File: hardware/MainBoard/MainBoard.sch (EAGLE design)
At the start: 220 parts, among them J1 CON-71741-2184-BOT, J2 CON-71741-2184-TOP, J3 CON-FTSH-105-01-L-DV-K, J4 CON-ZX62R-B-5P, J5 CON-SMA, J6 CON-SMA, J7 CON-RJ45-J0G-0007NL, J8 SWITCH-CJS-1200-1200, M1 MOUNT-HOLE3.3, M2 MOUNT-HOLE3.3, M3 MOUNT-HOLE3.3, M4 MOUNT-HOLE3.3, M5 FIDUCIAL1X2, M6 FIDUCIAL1X2, M7 FIDUCIAL1X2, M8 FIDUCIAL1X2, Q1 MMBT3904, SW1 SWITCH-KSC-201J, SW2 SWITCH-KSC-201J, U1 A2F500M3G-FG256, U2 MAX19706-T4877-4, U3 MAX19706-T4877-4, U4 USBLC6-2SC6, U5 FT232HL, U6 DP83848C-VBH48A, U7 93LC56BT-OT, U8 DS1818-10-SOT-23, U9 LMV112, X1 FOX924B, X2 ECX-31B, X3 ASEM1-C, X5 ECX-42-120

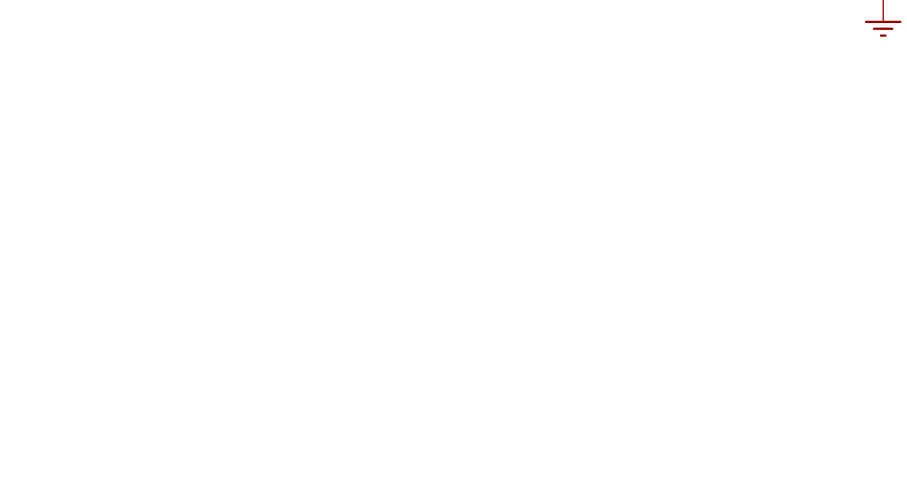
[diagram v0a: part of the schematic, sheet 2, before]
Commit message: Added decoupling capacitor to 1.5V supplies (3.3V IOB supply capacitors still missing).
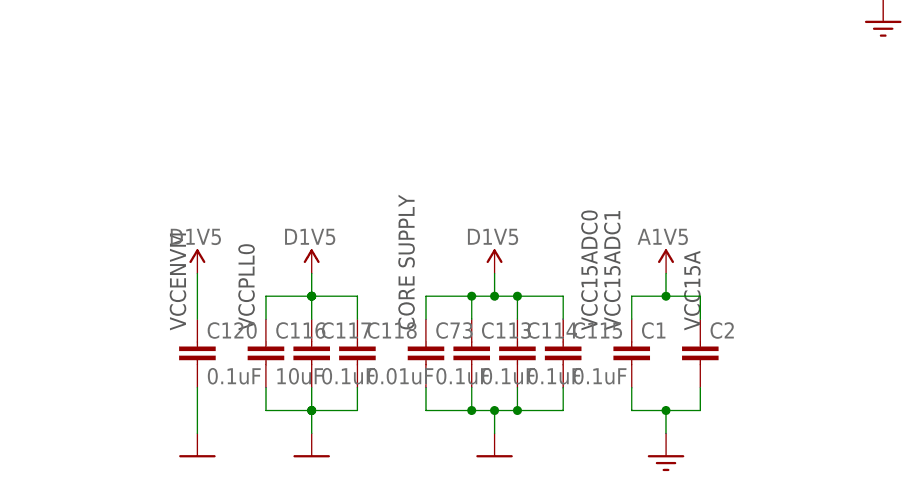
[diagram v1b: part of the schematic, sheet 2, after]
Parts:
- added C1, C2: (no value), MainBoard:C0402
- added C113, C114, C115, C117, C120, C73: 0.1uF, MainBoard:C0402
- added C116: 10uF, MainBoard:C0402
- added C118: 0.01uF, MainBoard:C0402
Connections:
- net A1V5: now also C1.1, C2.1
- net AGND: now also C1.2, C2.2
- net D1V5: now also C113.1, C114.1, C115.1, C116.1, C117.1, C118.1, C120.1, C73.1
- net DGND: now also C113.2, C114.2, C115.2, C116.2, C117.2, C118.2, C120.2, C73.2
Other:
- note added: "CORE SUPPLY"
- note added: "VCC15A"
- note added: "VCC15ADC0"
- note added: "VCC15ADC1"
- note added: "VCCENVM"
- note added: "VCCPLL0"
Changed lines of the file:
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@@
 <part name="U$69" library="MainBoard" deviceset="D3V3" device=""/>
 <part name="U$80" library="MainBoard" deviceset="D1V5" device=""/>
+<part name="C1" library="MainBoard" deviceset="C" device="0402"/>
+<part name="C2" library="MainBoard" deviceset="C" device="0402"/>
+<part name="U$81" library="MainBoard" deviceset="AGND" device=""/>
+<part name="U$88" library="MainBoard" deviceset="A1V5" device=""/>
+<part name="U$92" library="MainBoard" deviceset="D1V5" device=""/>
+<part name="C73" library="MainBoard" deviceset="C" device="0402" value="0.1uF"/>
+<part name="C113" library="MainBoard" deviceset="C" device="0402" value="0.1uF"/>
+<part name="C114" library="MainBoard" deviceset="C" device="0402" value="0.1uF"/>
+<part name="C115" library="MainBoard" deviceset="C" device="0402" value="0.1uF"/>
+<part name="U$126" library="MainBoard" deviceset="DGND" device=""/>
+<part name="U$135" library="MainBoard" deviceset="D1V5" device=""/>
+<part name="C116" library="MainBoard" deviceset="C" device="0402" value="10uF"/>
+<part name="C117" library="MainBoard" deviceset="C" device="0402" value="0.1uF"/>
+<part name="C118" library="MainBoard" deviceset="C" device="0402" value="0.01uF"/>
+<part name="U$136" library="MainBoard" deviceset="DGND" device=""/>
+<part name="U$137" library="MainBoard" deviceset="D1V5" device=""/>
+<part name="C120" library="MainBoard" deviceset="C" device="0402" value="0.1uF"/>
+<part name="U$138" library="MainBoard" deviceset="DGND" device=""/>
 </parts>
 <sheets>
@@
 <text x="182.88" y="111.76" size="2.54" layer="97">ANALOG-SUPPLY</text>
 <text x="53.34" y="78.74" size="50.8" layer="208">SUP</text>
-<rectangle x1="218.44" y1="143.51" x2="226.06" y2="146.05" layer="101"/>
+<rectangle x1="223.52" y1="143.51" x2="231.14" y2="146.05" layer="101"/>
 <rectangle x1="167.64" y1="120.65" x2="175.26" y2="123.19" layer="101"/>
+<text x="138.43" y="31.75" size="1.778" layer="97" rot="R90">VCC15ADC0</text>
+<text x="140.97" y="31.75" size="1.778" layer="97" rot="R90">VCC15ADC1</text>
+<text x="149.86" y="31.75" size="1.778" layer="97" rot="R90">VCC15A</text>
+<rectangle x1="137.16" y1="12.7" x2="157.48" y2="48.26" layer="116"/>
+<text x="118.11" y="31.75" size="1.778" layer="97" rot="R90">CORE SUPPLY</text>
+<text x="100.33" y="31.75" size="1.778" layer="97" rot="R90">VCCPLL0</text>
+<text x="92.71" y="31.75" size="1.778" layer="97" rot="R90">VCCENVM</text>
+<rectangle x1="86.36" y1="15.24" x2="116.84" y2="45.72" layer="116"/>
 </plain>
 <instances>
@@
 <instance part="U$69" gate="G$1" x="162.56" y="124.46"/>
 <instance part="U$80" gate="G$1" x="233.68" y="147.32"/>
+<instance part="C1" gate="G$1" x="142.24" y="30.48"/>
+<instance part="C2" gate="G$1" x="149.86" y="30.48"/>
+<instance part="U$81" gate="G$1" x="146.05" y="17.78"/>
+<instance part="U$88" gate="G$1" x="146.05" y="38.1"/>
+<instance part="U$92" gate="G$1" x="127" y="38.1"/>
+<instance part="C73" gate="G$1" x="119.38" y="30.48"/>
+<instance part="C113" gate="G$1" x="124.46" y="30.48"/>
+<instance part="C114" gate="G$1" x="129.54" y="30.48"/>
+<instance part="C115" gate="G$1" x="134.62" y="30.48"/>
+<instance part="U$126" gate="G$1" x="127" y="17.78"/>
+<instance part="U$135" gate="G$1" x="106.68" y="38.1"/>
+<instance part="C116" gate="G$1" x="101.6" y="30.48"/>
+<instance part="C117" gate="G$1" x="106.68" y="30.48"/>
+<instance part="C118" gate="G$1" x="111.76" y="30.48"/>
+<instance part="U$136" gate="G$1" x="106.68" y="17.78"/>
+<instance part="U$137" gate="G$1" x="93.98" y="38.1"/>
+<instance part="C120" gate="G$1" x="93.98" y="30.48"/>
+<instance part="U$138" gate="G$1" x="93.98" y="17.78"/>
 </instances>
 <busses>
@@
 <junction x="149.86" y="101.6"/>
 </segment>
+<segment>
+<pinref part="C73" gate="G$1" pin="2"/>
+<wire x1="119.38" y1="25.4" x2="119.38" y2="22.86" width="0.1524" layer="91"/>
+<wire x1="119.38" y1="22.86" x2="124.46" y2="22.86" width="0.1524" layer="91"/>
+<pinref part="C115" gate="G$1" pin="2"/>
+<wire x1="124.46" y1="22.86" x2="127" y2="22.86" width="0.1524" layer="91"/>
+<wire x1="127" y1="22.86" x2="129.54" y2="22.86" width="0.1524" layer="91"/>
+<wire x1="129.54" y1="22.86" x2="134.62" y2="22.86" width="0.1524" layer="91"/>
+<wire x1="134.62" y1="22.86" x2="134.62" y2="25.4" width="0.1524" layer="91"/>
+<pinref part="C113" gate="G$1" pin="2"/>
+<wire x1="124.46" y1="25.4" x2="124.46" y2="22.86" width="0.1524" layer="91"/>
+<pinref part="C114" gate="G$1" pin="2"/>
+<wire x1="129.54" y1="25.4" x2="129.54" y2="22.86" width="0.1524" layer="91"/>
+<wire x1="127" y1="22.86" x2="127" y2="20.32" width="0.1524" layer="91"/>
+<pinref part="U$126" gate="G$1" pin="DGND"/>
+<junction x="124.46" y="22.86"/>
+<junction x="127" y="22.86"/>
+<junction x="129.54" y="22.86"/>
+</segment>
+<segment>
+<pinref part="C116" gate="G$1" pin="2"/>
+<wire x1="101.6" y1="25.4" x2="101.6" y2="22.86" width="0.1524" layer="91"/>
+<wire x1="101.6" y1="22.86" x2="106.68" y2="22.86" width="0.1524" layer="91"/>
+<wire x1="106.68" y1="22.86" x2="111.76" y2="22.86" width="0.1524" layer="91"/>
+<pinref part="C117" gate="G$1" pin="2"/>
+<wire x1="106.68" y1="25.4" x2="106.68" y2="22.86" width="0.1524" layer="91"/>
+<pinref part="C118" gate="G$1" pin="2"/>
+<wire x1="111.76" y1="25.4" x2="111.76" y2="22.86" width="0.1524" layer="91"/>
+<wire x1="106.68" y1="22.86" x2="106.68" y2="20.32" width="0.1524" layer="91"/>
+<pinref part="U$136" gate="G$1" pin="DGND"/>
+<junction x="106.68" y="22.86"/>
+<junction x="106.68" y="22.86"/>
+</segment>
+<segment>
+<pinref part="C120" gate="G$1" pin="2"/>
+<wire x1="93.98" y1="25.4" x2="93.98" y2="20.32" width="0.1524" layer="91"/>
+<pinref part="U$138" gate="G$1" pin="DGND"/>
+</segment>
 </net>
 <net name="D1V5" class="0">
@@
 <wire x1="233.68" y1="144.78" x2="233.68" y2="147.32" width="0.1524" layer="91"/>
 <pinref part="U$80" gate="G$1" pin="D1V5"/>
+</segment>
+<segment>
+<pinref part="U$92" gate="G$1" pin="D1V5"/>
+<wire x1="127" y1="38.1" x2="127" y2="35.56" width="0.1524" layer="91"/>
+<wire x1="127" y1="35.56" x2="124.46" y2="35.56" width="0.1524" layer="91"/>
+<wire x1="124.46" y1="35.56" x2="119.38" y2="35.56" width="0.1524" layer="91"/>
+<wire x1="127" y1="35.56" x2="129.54" y2="35.56" width="0.1524" layer="91"/>
+<pinref part="C73" gate="G$1" pin="1"/>
+<wire x1="129.54" y1="35.56" x2="134.62" y2="35.56" width="0.1524" layer="91"/>
+<wire x1="119.38" y1="33.02" x2="119.38" y2="35.56" width="0.1524" layer="91"/>
+<pinref part="C113" gate="G$1" pin="1"/>
+<wire x1="124.46" y1="33.02" x2="124.46" y2="35.56" width="0.1524" layer="91"/>
+<pinref part="C114" gate="G$1" pin="1"/>
+<wire x1="129.54" y1="33.02" x2="129.54" y2="35.56" width="0.1524" layer="91"/>
+<pinref part="C115" gate="G$1" pin="1"/>
+<wire x1="134.62" y1="33.02" x2="134.62" y2="35.56" width="0.1524" layer="91"/>
+<junction x="124.46" y="35.56"/>
+<junction x="127" y="35.56"/>
+<junction x="129.54" y="35.56"/>
+</segment>
+<segment>
+<pinref part="U$135" gate="G$1" pin="D1V5"/>
+<wire x1="106.68" y1="38.1" x2="106.68" y2="35.56" width="0.1524" layer="91"/>
+<wire x1="106.68" y1="35.56" x2="101.6" y2="35.56" width="0.1524" layer="91"/>
+<wire x1="106.68" y1="35.56" x2="111.76" y2="35.56" width="0.1524" layer="91"/>
+<pinref part="C116" gate="G$1" pin="1"/>
+<wire x1="101.6" y1="33.02" x2="101.6" y2="35.56" width="0.1524" layer="91"/>
+<pinref part="C117" gate="G$1" pin="1"/>
+<wire x1="106.68" y1="33.02" x2="106.68" y2="35.56" width="0.1524" layer="91"/>
+<pinref part="C118" gate="G$1" pin="1"/>
+<wire x1="111.76" y1="33.02" x2="111.76" y2="35.56" width="0.1524" layer="91"/>
+<junction x="106.68" y="35.56"/>
+<junction x="106.68" y="35.56"/>
+</segment>
+<segment>
+<pinref part="U$137" gate="G$1" pin="D1V5"/>
+<pinref part="C120" gate="G$1" pin="1"/>
+<wire x1="93.98" y1="33.02" x2="93.98" y2="38.1" width="0.1524" layer="91"/>
 </segment>
 </net>
@@
 <junction x="226.06" y="71.12"/>
 </segment>
+<segment>
+<pinref part="C2" gate="G$1" pin="2"/>
+<pinref part="C1" gate="G$1" pin="2"/>
+<wire x1="142.24" y1="25.4" x2="142.24" y2="22.86" width="0.1524" layer="91"/>
+<wire x1="142.24" y1="22.86" x2="146.05" y2="22.86" width="0.1524" layer="91"/>
+<wire x1="146.05" y1="22.86" x2="149.86" y2="22.86" width="0.1524" layer="91"/>
+<wire x1="149.86" y1="22.86" x2="149.86" y2="25.4" width="0.1524" layer="91"/>
+<pinref part="U$81" gate="G$1" pin="AGND"/>
+<wire x1="146.05" y1="20.32" x2="146.05" y2="22.86" width="0.1524" layer="91"/>
+<junction x="146.05" y="22.86"/>
+</segment>
 </net>
 <net name="A1V5" class="0">
@@
 <junction x="226.06" y="157.48"/>
 </segment>
+<segment>
+<pinref part="C1" gate="G$1" pin="1"/>
+<wire x1="142.24" y1="33.02" x2="142.24" y2="35.56" width="0.1524" layer="91"/>
+<wire x1="142.24" y1="35.56" x2="146.05" y2="35.56" width="0.1524" layer="91"/>
+<wire x1="146.05" y1="35.56" x2="146.05" y2="38.1" width="0.1524" layer="91"/>
+<pinref part="U$88" gate="G$1" pin="A1V5"/>
+<pinref part="C2" gate="G$1" pin="1"/>
+<wire x1="149.86" y1="33.02" x2="149.86" y2="35.56" width="0.1524" layer="91"/>
+<wire x1="149.86" y1="35.56" x2="146.05" y2="35.56" width="0.1524" layer="91"/>
+<junction x="146.05" y="35.56"/>
+</segment>
 </net>

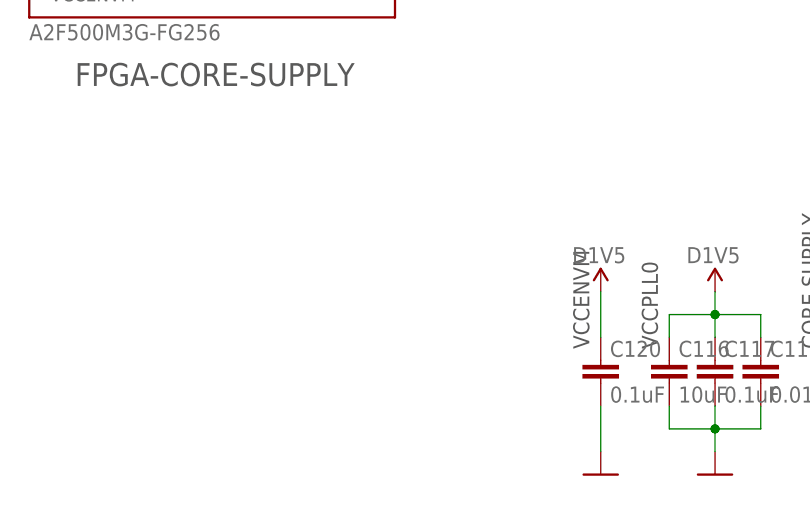
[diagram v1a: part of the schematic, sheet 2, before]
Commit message: 
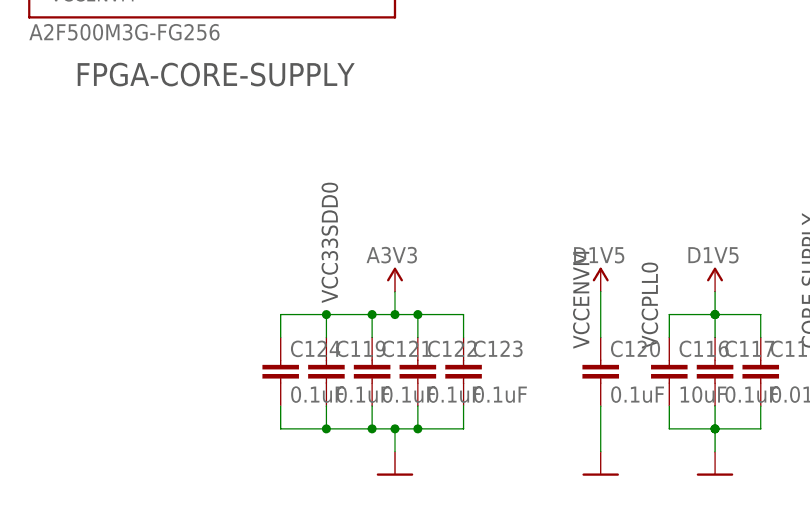
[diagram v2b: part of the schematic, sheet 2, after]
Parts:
- added C119, C121, C122, C123, C124: 0.1uF, MainBoard:C0402
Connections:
- net A3V3: now also C119.1, C121.1, C122.1, C123.1, C124.1
- net DGND: now also C119.2, C121.2, C122.2, C123.2, C124.2
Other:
- note added: "VCC33SDD0"
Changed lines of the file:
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@@
 <part name="C120" library="MainBoard" deviceset="C" device="0402" value="0.1uF"/>
 <part name="U$138" library="MainBoard" deviceset="DGND" device=""/>
+<part name="C119" library="MainBoard" deviceset="C" device="0402" value="0.1uF"/>
+<part name="C121" library="MainBoard" deviceset="C" device="0402" value="0.1uF"/>
+<part name="C122" library="MainBoard" deviceset="C" device="0402" value="0.1uF"/>
+<part name="C123" library="MainBoard" deviceset="C" device="0402" value="0.1uF"/>
+<part name="U$140" library="MainBoard" deviceset="DGND" device=""/>
+<part name="U$139" library="MainBoard" deviceset="A3V3" device=""/>
+<part name="C124" library="MainBoard" deviceset="C" device="0402" value="0.1uF"/>
 </parts>
 <sheets>
@@
 <text x="92.71" y="31.75" size="1.778" layer="97" rot="R90">VCCENVM</text>
 <rectangle x1="86.36" y1="15.24" x2="116.84" y2="45.72" layer="116"/>
+<rectangle x1="12.7" y1="66.04" x2="88.9" y2="99.06" layer="116"/>
+<rectangle x1="200.66" y1="147.32" x2="228.6" y2="165.1" layer="116"/>
+<rectangle x1="96.52" y1="83.82" x2="154.94" y2="165.1" layer="116"/>
+<rectangle x1="165.1" y1="53.34" x2="236.22" y2="104.14" layer="116"/>
+<rectangle x1="218.44" y1="109.22" x2="236.22" y2="124.46" layer="116"/>
+<text x="64.77" y="36.83" size="1.778" layer="97" rot="R90">VCC33SDD0</text>
 </plain>
 <instances>
@@
 <instance part="C120" gate="G$1" x="93.98" y="30.48"/>
 <instance part="U$138" gate="G$1" x="93.98" y="17.78"/>
+<instance part="C119" gate="G$1" x="63.5" y="30.48"/>
+<instance part="C121" gate="G$1" x="68.58" y="30.48"/>
+<instance part="C122" gate="G$1" x="73.66" y="30.48"/>
+<instance part="C123" gate="G$1" x="78.74" y="30.48"/>
+<instance part="U$140" gate="G$1" x="71.12" y="17.78"/>
+<instance part="U$139" gate="G$1" x="71.12" y="38.1"/>
+<instance part="C124" gate="G$1" x="58.42" y="30.48"/>
 </instances>
 <busses>
@@
 <pinref part="U$138" gate="G$1" pin="DGND"/>
 </segment>
+<segment>
+<pinref part="C119" gate="G$1" pin="2"/>
+<wire x1="63.5" y1="25.4" x2="63.5" y2="22.86" width="0.1524" layer="91"/>
+<wire x1="63.5" y1="22.86" x2="68.58" y2="22.86" width="0.1524" layer="91"/>
+<pinref part="C123" gate="G$1" pin="2"/>
+<wire x1="68.58" y1="22.86" x2="71.12" y2="22.86" width="0.1524" layer="91"/>
+<wire x1="71.12" y1="22.86" x2="73.66" y2="22.86" width="0.1524" layer="91"/>
+<wire x1="73.66" y1="22.86" x2="78.74" y2="22.86" width="0.1524" layer="91"/>
+<wire x1="78.74" y1="22.86" x2="78.74" y2="25.4" width="0.1524" layer="91"/>
+<pinref part="C121" gate="G$1" pin="2"/>
+<wire x1="68.58" y1="25.4" x2="68.58" y2="22.86" width="0.1524" layer="91"/>
+<pinref part="C122" gate="G$1" pin="2"/>
+<wire x1="73.66" y1="25.4" x2="73.66" y2="22.86" width="0.1524" layer="91"/>
+<wire x1="71.12" y1="22.86" x2="71.12" y2="20.32" width="0.1524" layer="91"/>
+<pinref part="U$140" gate="G$1" pin="DGND"/>
+<junction x="68.58" y="22.86"/>
+<junction x="71.12" y="22.86"/>
+<junction x="73.66" y="22.86"/>
+<pinref part="C124" gate="G$1" pin="2"/>
+<wire x1="58.42" y1="25.4" x2="58.42" y2="22.86" width="0.1524" layer="91"/>
+<wire x1="58.42" y1="22.86" x2="63.5" y2="22.86" width="0.1524" layer="91"/>
+<junction x="63.5" y="22.86"/>
+</segment>
 </net>
 <net name="D1V5" class="0">
@@
 <junction x="170.18" y="137.16"/>
 </segment>
+<segment>
+<wire x1="71.12" y1="38.1" x2="71.12" y2="35.56" width="0.1524" layer="91"/>
+<wire x1="71.12" y1="35.56" x2="68.58" y2="35.56" width="0.1524" layer="91"/>
+<wire x1="68.58" y1="35.56" x2="63.5" y2="35.56" width="0.1524" layer="91"/>
+<wire x1="71.12" y1="35.56" x2="73.66" y2="35.56" width="0.1524" layer="91"/>
+<pinref part="C119" gate="G$1" pin="1"/>
+<wire x1="73.66" y1="35.56" x2="78.74" y2="35.56" width="0.1524" layer="91"/>
+<wire x1="63.5" y1="33.02" x2="63.5" y2="35.56" width="0.1524" layer="91"/>
+<pinref part="C121" gate="G$1" pin="1"/>
+<wire x1="68.58" y1="33.02" x2="68.58" y2="35.56" width="0.1524" layer="91"/>
+<pinref part="C122" gate="G$1" pin="1"/>
+<wire x1="73.66" y1="33.02" x2="73.66" y2="35.56" width="0.1524" layer="91"/>
+<pinref part="C123" gate="G$1" pin="1"/>
+<wire x1="78.74" y1="33.02" x2="78.74" y2="35.56" width="0.1524" layer="91"/>
+<junction x="68.58" y="35.56"/>
+<junction x="71.12" y="35.56"/>
+<junction x="73.66" y="35.56"/>
+<pinref part="U$139" gate="G$1" pin="A3V3"/>
+<pinref part="C124" gate="G$1" pin="1"/>
+<wire x1="58.42" y1="33.02" x2="58.42" y2="35.56" width="0.1524" layer="91"/>
+<wire x1="58.42" y1="35.56" x2="63.5" y2="35.56" width="0.1524" layer="91"/>
+<junction x="63.5" y="35.56"/>
+</segment>
 </net>

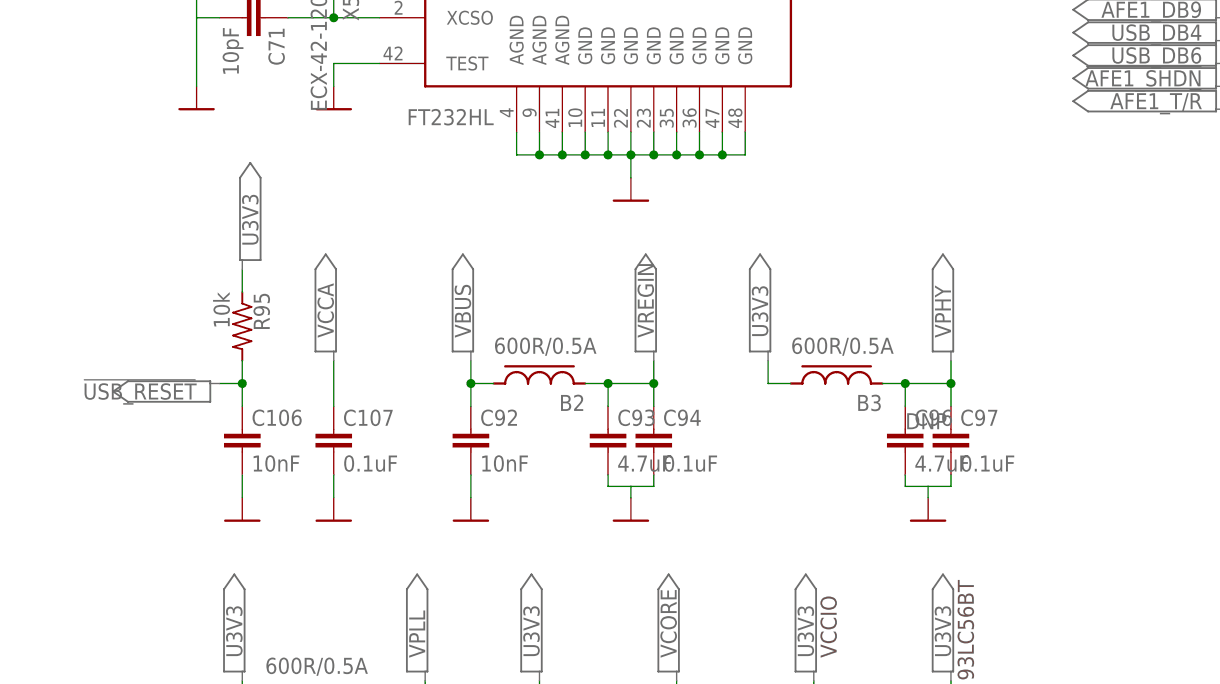
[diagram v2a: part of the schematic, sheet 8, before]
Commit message: USB routing optimization back-up.
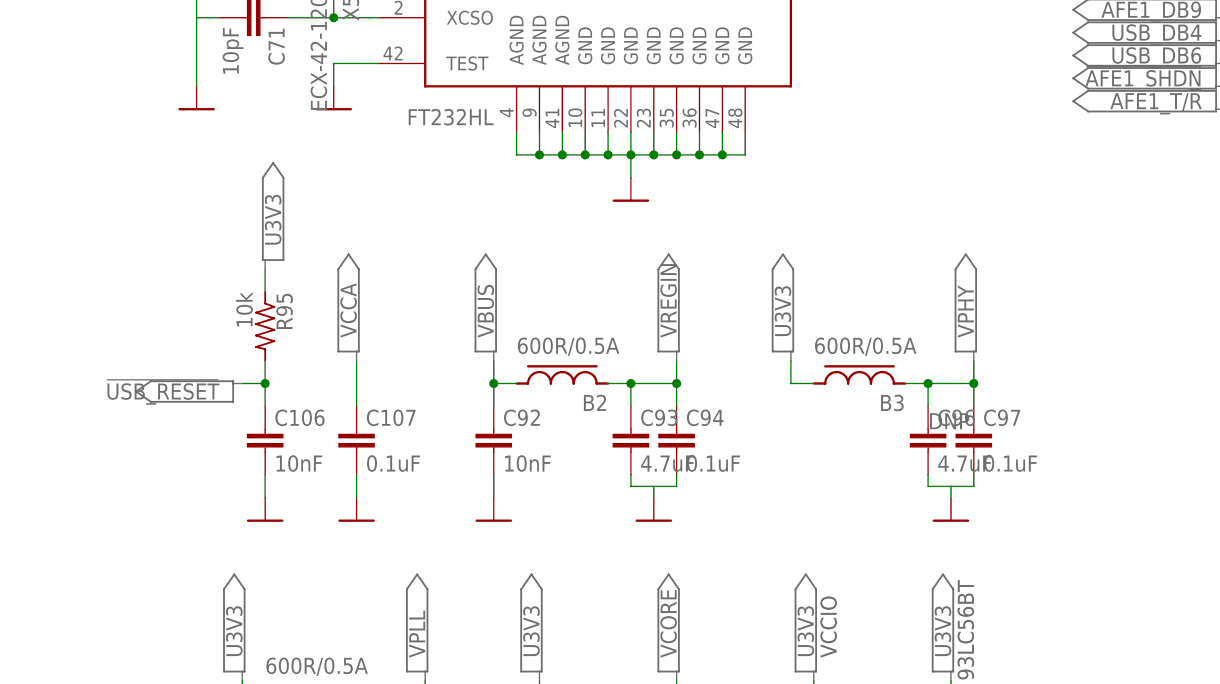
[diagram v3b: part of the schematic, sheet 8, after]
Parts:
- added C125, C126: (no value), MainBoard:C0402
- added C127: 0.1uF, MainBoard:C0402
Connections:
- removed net N$15: J4.D-, U4.IO1@2
- removed net N$19: J4.D+, U4.IO2@2
- removed net N$25: R55.1, U4.IO1@1
- removed net N$26: R56.1, U4.IO2@1
- new net USBDM-IN: J4.D-, U4.IO1@1
- new net USBDM-OUT: R55.1, U4.IO1@2
- new net USBDP-IN: J4.D+, U4.IO2@1
- new net USBDP-OUT: R56.1, U4.IO2@2
- net AGND: now also C119.2, C121.2, C122.2, C123.2, C124.2
- net DGND: now also C127.2; no longer C119.2, C121.2, C122.2, C123.2, C124.2
- net VBUS: now also C127.1
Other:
- note added: "Place close to USBLC6 output"
- moved on the sheet: B2, B3, C106, C107, C92, C93, C94, C96, C97, R55, R56, R95
